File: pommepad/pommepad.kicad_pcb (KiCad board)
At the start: 2 copper layers, 90.9 x 76.6 mm, 27 parts, among them SW1 SW_Push, SW2 SW_Push, SW3 SW_Push, SW4 SW_Push, SW5 SW_Push, SW6 SW_Push, U1 XIAO-RP2040-DIP, U2 OLED_0.91_128x32

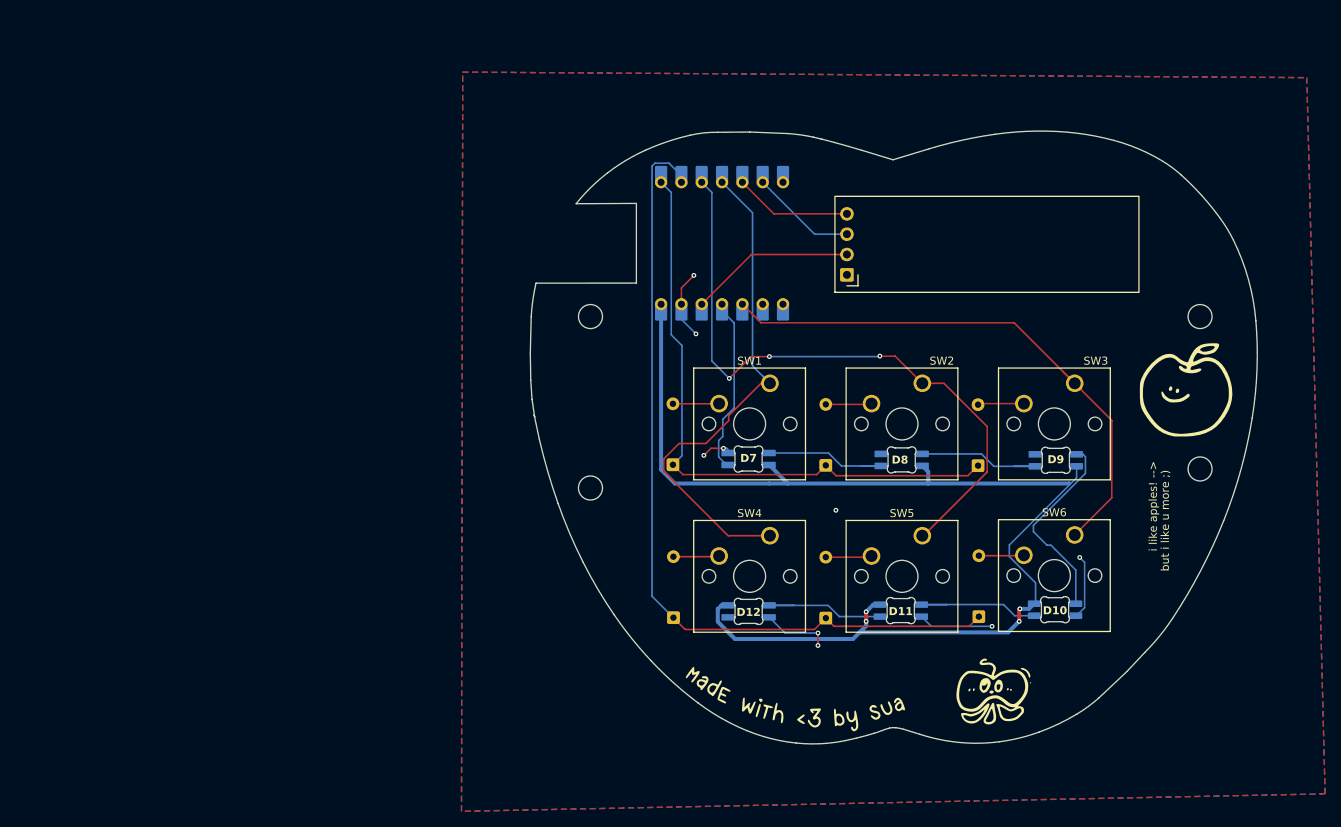
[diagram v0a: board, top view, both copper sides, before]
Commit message: silkscreen done
done all my silkscreen ! this is probably gonna be subject to change because some of it is kinda corny but ill come back. soon... also generated step file to start cad
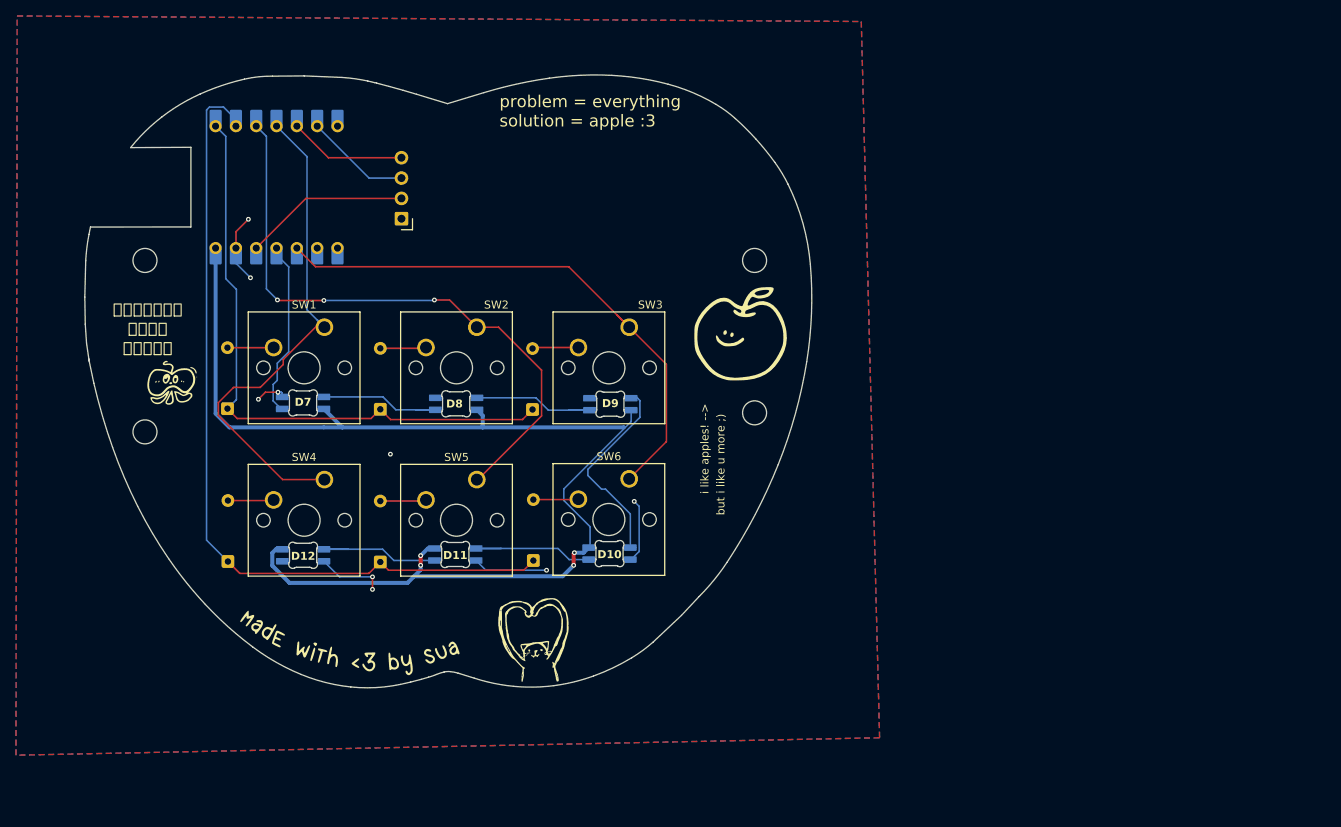
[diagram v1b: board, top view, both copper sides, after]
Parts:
- removed the G*** at (209.8, 131.2)
- added G***: LOGO, LOGO, F.Cu at (152.2, 121.0)
- added G***: LOGO, LOGO, F.Cu at (107.1, 92.4)
- added G***: LOGO, LOGO, B.Cu at (148.0, 71.7)
- moved D6 56.1 mm to (152.2, 114.3)
- moved REF** 56.1 mm to (179.9, 76.8)
- moved REF** 56.1 mm to (179.9, 95.9)
- moved SW2 56.1 mm to (142.6, 90.2)
- moved SW5 56.1 mm to (142.6, 109.3)
- moved D4 56.1 mm to (114.1, 114.4)
- moved D10 56.1 mm to (161.8, 113.6)
- moved D11 56.1 mm to (142.5, 113.7)
- moved D12 56.1 mm to (123.5, 113.8)
- moved D2 56.1 mm to (133.1, 95.4)
- moved D3 56.1 mm to (152.1, 95.4)
- moved D8 56.1 mm to (142.6, 94.6)
- moved D9 56.1 mm to (161.9, 94.7)
- moved G*** 56.1 mm to (129.6, 125.7)
- moved G*** 56.1 mm to (178.4, 85.9)
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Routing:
- net COL2: track 80.9 -> 77.5 mm
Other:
- board text added: "problem = everything solution = apple :3"
- board text added: "看起来很简单 做起来完全不是那回事 每一步都在猜 但也走到了这里 but somehow it worked ?"
- board text added: "苹果的糖分很高 但是它没 比你更甜哦"
